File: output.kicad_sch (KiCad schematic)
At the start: 20 parts, among them SW7 SW_SPDT, U37 74LS86, U38 74LS139, U39 SN74LS74AN, U40 7SEGMENT_CC, U41 7SEGMENT_CC, U42 7SEGMENT_CC, U43 7SEGMENT_CC, U44 74LS273, U45 28C16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

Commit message: Output modified
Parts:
- removed U37: 74LS86, Package_DIP:DIP-14_W7.62mm, symbol 8bit-computer-rescue:74LS86-8bit-computer-rescue
- added U37: 74LS86, symbol 74xx:74LS86
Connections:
- net GND: now also U37.7 (GND)
- net VCC: now also U37.14 (VCC)
- net at U38.3 (A1), U39.5 (1Q), U45.22 (A9): now also U37.2
- net at U38.2 (A0), U39.9 (2Q), U45.23 (A8): now also U37.1
- net at U39.12 (2D): now also U37.3
- no-connect marks 18 -> 27

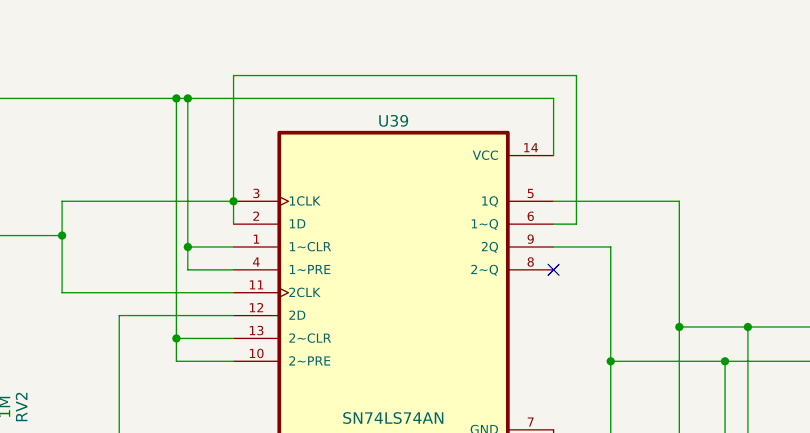
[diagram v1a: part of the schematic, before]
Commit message: Final version
PCB update is missing
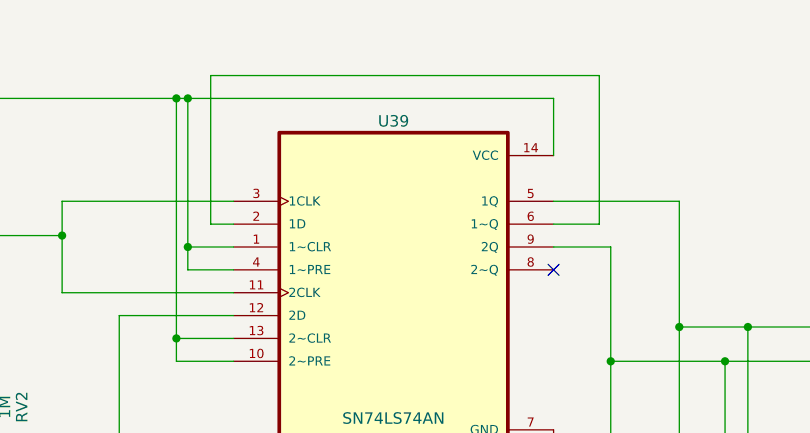
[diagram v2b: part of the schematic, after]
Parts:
- U37: footprint (none) -> Package_DIP:DIP-14_W7.62mm
- U39: footprint SN74LS74AN:DIP794W45P254L1969H508Q14 -> 8bit-custom-footprints:DIP794W45P254L1969H508Q14
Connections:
- net at U39.11 (2CLK), U39.3 (1CLK), U54.3 (Q): no longer U39.2 (1D), U39.6 (1~Q)
- new net: U39.2 (1D), U39.6 (1~Q)
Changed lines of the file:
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@@
   (junction (at 228.6 106.68) (diameter 0) (color 0 0 0 0)
-  )
-  (junction (at 97.79 33.02) (diameter 0) (color 0 0 0 0)
   )
   (junction (at 181.61 129.54) (diameter 0) (color 0 0 0 0)
@@
     (stroke (width 0) (type default))
   )
+  (wire (pts (xy 95.25 35.56) (xy 97.79 35.56))
+    (stroke (width 0) (type default))
+  )
   (wire (pts (xy 172.72 114.3) (xy 196.85 114.3))
     (stroke (width 0) (type default))
@@
     (stroke (width 0) (type default))
   )
+  (wire (pts (xy 95.25 19.05) (xy 95.25 35.56))
+    (stroke (width 0) (type default))
+  )
   (wire (pts (xy 184.15 66.04) (xy 209.55 66.04))
     (stroke (width 0) (type default))
@@
     (stroke (width 0) (type default))
   )
-  (wire (pts (xy 97.79 35.56) (xy 97.79 33.02))
-    (stroke (width 0) (type default))
-  )
   (wire (pts (xy 157.48 114.3) (xy 172.72 114.3))
     (stroke (width 0) (type default))
@@
     (stroke (width 0) (type default))
   )
-  (wire (pts (xy 133.35 35.56) (xy 135.89 35.56))
+  (wire (pts (xy 133.35 35.56) (xy 138.43 35.56))
     (stroke (width 0) (type default))
   )
@@
     (stroke (width 0) (type default))
   )
-  (wire (pts (xy 97.79 19.05) (xy 135.89 19.05))
+  (wire (pts (xy 95.25 19.05) (xy 138.43 19.05))
     (stroke (width 0) (type default))
   )
@@
     (stroke (width 0) (type default))
   )
-  (wire (pts (xy 97.79 33.02) (xy 97.79 19.05))
-    (stroke (width 0) (type default))
-  )
   (wire (pts (xy 257.81 69.85) (xy 257.81 71.12))
     (stroke (width 0) (type default))
@@
     (stroke (width 0) (type default))
   )
-  (wire (pts (xy 135.89 19.05) (xy 135.89 35.56))
+  (wire (pts (xy 138.43 19.05) (xy 138.43 35.56))
     (stroke (width 0) (type default))
   )
@@
       (effects (font (size 1.27 1.27)))
     )
-    (property "Footprint" "" (at 27.94 193.04 0)
+    (property "Footprint" "Package_DIP:DIP-14_W7.62mm" (at 27.94 193.04 0)
       (effects (font (size 1.27 1.27)) hide)
     )
@@
       (effects (font (size 1.27 1.27)))
     )
-    (property "Footprint" "" (at 46.99 179.07 0)
+    (property "Footprint" "Package_DIP:DIP-14_W7.62mm" (at 46.99 179.07 0)
       (effects (font (size 1.27 1.27)) hide)
     )
@@
       (effects (font (size 1.27 1.27)))
     )
-    (property "Footprint" "" (at 115.57 69.85 0)
+    (property "Footprint" "Package_DIP:DIP-14_W7.62mm" (at 115.57 69.85 0)
       (effects (font (size 1.27 1.27)) hide)
     )
@@
       (effects (font (size 1.27 1.27)))
     )
-    (property "Footprint" "" (at 50.8 193.04 0)
+    (property "Footprint" "Package_DIP:DIP-14_W7.62mm" (at 50.8 193.04 0)
       (effects (font (size 1.27 1.27)) hide)
     )
@@
       (effects (font (size 1.27 1.27)))
     )
-    (property "Footprint" "SN74LS74AN:DIP794W45P254L1969H508Q14" (at 115.57 43.18 0)
+    (property "Footprint" "8bit-custom-footprints:DIP794W45P254L1969H508Q14" (at 115.57 43.18 0) (do_not_autoplace)
       (effects (font (size 1.27 1.27)) (justify bottom) hide)
     )
@@
       (effects (font (size 1.27 1.27)))
     )
-    (property "Footprint" "" (at 27.94 179.07 0)
-      (effects (font (size 1.27 1.27)) hide)
-    )
+    (property "Footprint" "Package_DIP:DIP-14_W7.62mm" (at 27.94 179.07 0)
+      (effects (font (size 1.27 1.27)) hide)
+    )

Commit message: Updated version
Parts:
- removed C25: 0.01µF, Capacitor_THT:C_Disc_D4.3mm_W1.9mm_P5.00mm, symbol Device:C
- removed C26: 1µF, Capacitor_THT:CP_Radial_D5.0mm_P2.00mm, symbol 8bit-computer-rescue:CP1-Device
- removed R105, R106: 1K, Resistor_THT:R_Axial_DIN0207_L6.3mm_D2.5mm_P7.62mm_Horizontal, symbol Device:R
- removed U37: 74LS86, Package_DIP:DIP-14_W7.62mm, symbol 74xx:74LS86
- removed U39: SN74LS74AN, 8bit-custom-footprints:DIP794W45P254L1969H508Q14, symbol SN74LS74AN:SN74LS74AN
- removed U54: LM555, Package_DIP:DIP-8_W7.62mm, symbol 8bit-computer-rescue:LM555-8bit-computer-rescue
- added C8: 0.01µF, Capacitor_THT:C_Disc_D4.3mm_W1.9mm_P5.00mm, symbol Device:C
- added C9: 1µF, Capacitor_THT:CP_Radial_D5.0mm_P2.00mm, symbol 8bit-computer-rescue:CP1-Device
- added R65, R66: 1K, Resistor_THT:R_Axial_DIN0207_L6.3mm_D2.5mm_P7.62mm_Horizontal, symbol Device:R
- added U37: 8bit-computer-rescue:74LS161, symbol 8bit-computer-rescue:74LS161-8bit-computer-rescue
- added U39: LM555, Package_DIP:DIP-8_W7.62mm, symbol 8bit-computer-rescue:LM555-8bit-computer-rescue
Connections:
- net GND: now also C8.2, C9.2, U37.8 (GND), U39.1 (GND)
- net VCC: now also R65.1, U37.1 (~{MR}), U37.10 (Cet), U37.16 (VCC), U37.7 (Cep), U37.9 (~{Pe}), U39.4 (R), U39.8 (VCC)
- net at U38.3 (A1), U45.22 (A9): now also U37.13 (Q1)
- net at U38.2 (A0), U45.23 (A8): now also U37.14 (Q0)
- net at RV2.1: now also C9.1, U39.2 (TR), U39.6 (THR)
- net at RV2.2: now also R66.1
- new net: R65.2, R66.2, U39.7 (DIS)
- new net: U37.2 (Cp), U39.3 (Q)
- new net: C8.1, U39.5 (CV)
- no-connect marks 27 -> 24
